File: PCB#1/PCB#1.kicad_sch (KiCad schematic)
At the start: 30 parts, among them J2 Conn_01x02, J3 Conn_02x18_Odd_Even, J4 Conn_02x18_Odd_Even, P1 USB_C_Plug_USB2.0, U1 RP2040, U2 ICM-20948, U3 NCP1117-3.3_SOT223, U4 W25Q128JVS, Y1 Crystal_GND24

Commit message: Add files via upload
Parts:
- added Cd12, Ci2: 10uF, symbol Device:C
- added U5: NCP1117-1.8_SOT223, Package_TO_SOT_SMD:SOT-223-3_TabPin2, symbol Regulator_Linear:NCP1117-1.8_SOT223
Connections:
- net +3.3V: now also Ci2.1, U5.3 (VI); no longer U2.13 (VDD)
- net +3V3: now also U2.13 (VDD)
- net GND: now also Cd12.2, Ci2.2, U5.1 (GND)
- net +1V8: now reaches U2.8 (VDDIO)
- net +1V8: now also Cd12.1, U5.2 (VO)
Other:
- note added: "Input Supply Converts 3.3v to 1.8v"

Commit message: Add files via upload
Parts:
- removed Cd2: 10uF, symbol Device:C
- removed J3, J4: Conn_02x18_Odd_Even, symbol Connector_Generic:Conn_02x18_Odd_Even
- added Cd13, Cd14, Cd15: 100nF, symbol Device:C
- added Cd16: 10uF, symbol Device:C
- added Q1: BSS138, Package_TO_SOT_SMD:SOT-23, symbol Transistor_FET:BSS138
- added R6, R7: 4.7k, symbol Device:R
- added U6: ISO1540, Package_SO:SOIC-8_3.9x4.9mm_P1.27mm, symbol Isolator:ISO1540
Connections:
- net GND is gone; now on net +1V8: Cc1.2, Cc2.2, Cd1.2, Cd10.2, Cd11.2, Cd12.2, Cd2.2, Cd3.2, Cd4.2, Cd5.2, Cd6.2, Cd7.2, Cd8.2, Cd9.2, Cf1.2, Ci1.2, Ci2.2, J2.2 (Pin_2), P1.A1 (GND), P1.A12 (GND), P1.B1 (GND), P1.B12 (GND), P1.S1 (SHIELD), R5.2, U1.57 (GND), U2.18 (GND), U2.20 (GND), U3.1 (GND), U4.4 (GND), U5.1 (GND), Y1.2, Y1.4
- net +1V8: now also U2.9 (SDO/AD0), Cd13.2, Cd14.1, Cd14.2, Cd15.2, Cd16.2, Q1.1 (G), R7.1, U6.4 (GND1), U6.5 (GND2), U6.8 (VCC2)
- net +3V3: now also Cd13.1, Cd16.1, U6.1 (VCC1)
- net at U2.10 (REGOUT): now also Cd15.1
- net at U2.22 (~{CS}): now also R7.2
- new net: Q1.2 (S), R6.1
- no-connect marks 1 -> 6
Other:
- note added: "Address to 0x68"
- note added: "Any GPIO"
- note added: "Data Level Shifter 1v8 to 3v3"
- note added: "I2C mode"
- note added: "INT"
- note added: "Interupt Level Shifter"
- note added: "SCL"
- note added: "SDA"
- moved on the sheet: Cc1, Cc2, Cd1, Cd10, Cd11, Cd2, Cd3, Cd4, Cd5, Cd6, Cd7, Cd8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

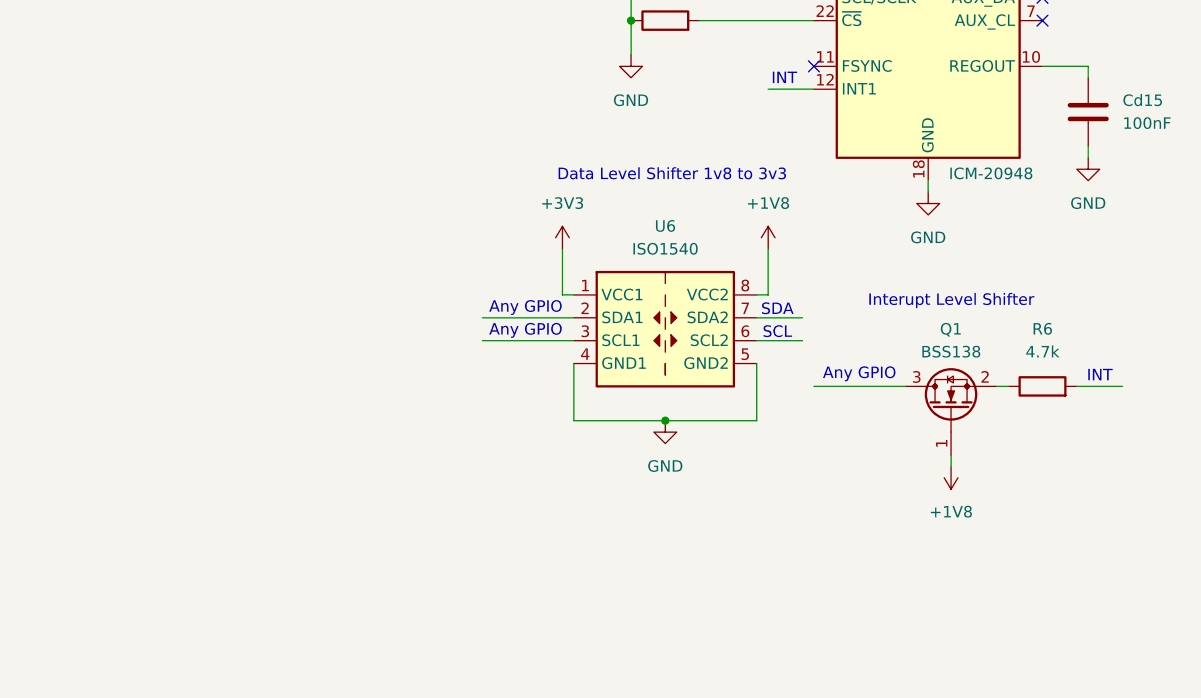
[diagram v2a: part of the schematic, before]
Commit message: Add files via upload
Fixed pull ups
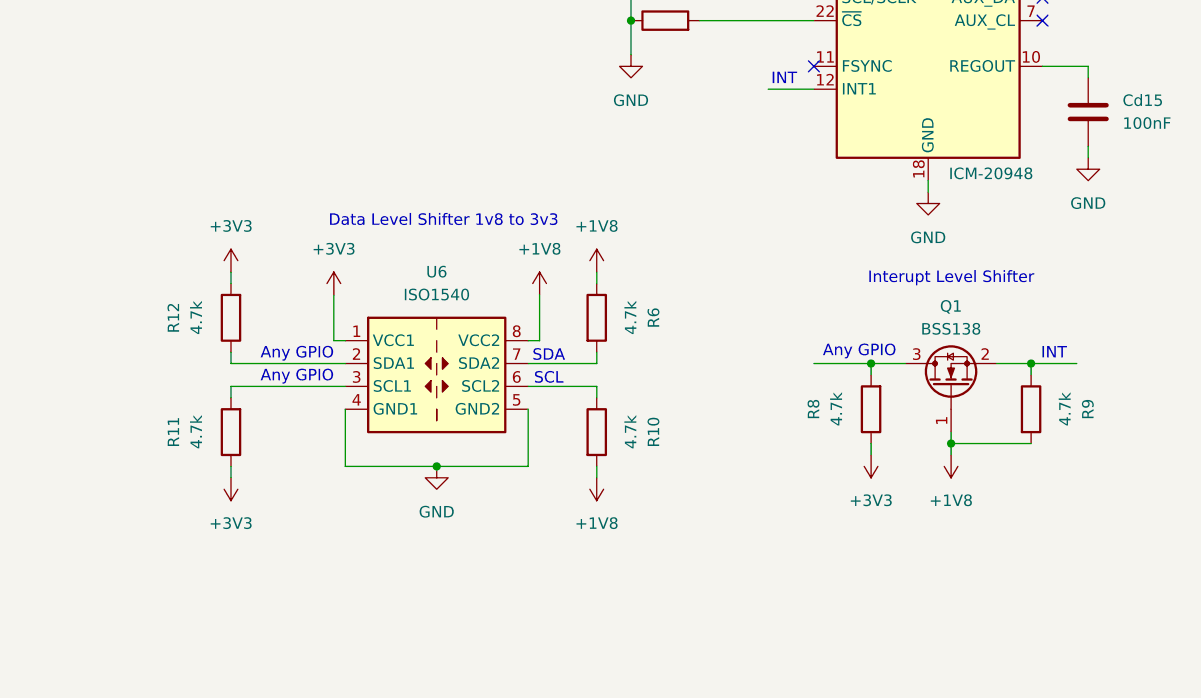
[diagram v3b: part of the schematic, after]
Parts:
- added R10, R11, R12, R8, R9: 4.7k, symbol Device:R
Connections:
- net +1V8: now also R6.1, R10.2, R9.2
- net +3V3: now also R11.1, R12.2, R8.1
- net at Q1.2 (S): now also R9.1; no longer R6.1
- net at Q1.3 (D): now also R8.2
- net at U6.2 (SDA1): now also R12.1
- net at U6.3 (SCL1): now also R11.2
- net at U6.6 (SCL2): now also R10.1
- net at U6.7 (SDA2): now also R6.2
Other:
- moved on the sheet: Q1, U6

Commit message: Add files via upload
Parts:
- removed R10, R11, R12, R6: 4.7k, symbol Device:R
- removed U6: ISO1540, Package_SO:SOIC-8_3.9x4.9mm_P1.27mm, symbol Isolator:ISO1540
- added Cd17, Cd18: 1uF, symbol Device:C
- added R13, R14, R15, R16: 4.7k, symbol Device:R
- added U7: MPL115A1, Package_LGA:NXP_LGA-8_3x5mm_P1.25mm_H1.2mm, symbol Sensor_Pressure:MPL115A1
- added U8: TCA9406DC, symbol Interface:TCA9406DC
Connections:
- net +1V8: now also U1.19 (TESTEN), Cd17.2, Cd18.2, R15.1, R16.2, U7.3 (GND), U8.2 (GND), U8.3 (VCCA), U8.6 (OE)
- net +3V3: now also Cd17.1, R13.2, R14.1, U7.1 (VDD), U8.7 (VCCB)
- new net: R13.1, U8.1 (SDA_B)
- new net: Cd18.1, U7.2 (CAP)
- new net: R14.2, U8.8 (SCL_B)
- new net: R15.2, U8.4 (SDA_A)
- new net: R16.1, U8.5 (SCL_A)
- no-connect marks 6 -> 7
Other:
- note added: "VDD"

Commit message: Add files via upload
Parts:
- added C24: 100nF, Capacitor_SMD:C_0603_1608Metric, symbol Device:C
- added R6: 27.4, Resistor_SMD:R_0603_1608Metric, symbol Device:R
- C1: renamed from Ci1; footprint (none) -> Capacitor_SMD:C_0603_1608Metric
- C10: renamed from Cd6; footprint (none) -> Capacitor_SMD:C_0603_1608Metric
- C11: renamed from Cd4; footprint (none) -> Capacitor_SMD:C_0603_1608Metric
- C12: renamed from Cd7; footprint (none) -> Capacitor_SMD:C_0603_1608Metric
- C13: renamed from Cd8; footprint (none) -> Capacitor_SMD:C_0603_1608Metric
- C14: renamed from Cd9; footprint (none) -> Capacitor_SMD:C_0603_1608Metric
- C15: renamed from Cd10; footprint (none) -> Capacitor_SMD:C_0603_1608Metric
- C16: renamed from Cd17; footprint (none) -> Capacitor_SMD:C_0603_1608Metric
- C17: renamed from Cd11; footprint (none) -> Capacitor_SMD:C_0603_1608Metric
- C18: renamed from Cd18; footprint (none) -> Capacitor_SMD:C_0603_1608Metric
- C19: renamed from Ci2; footprint (none) -> Capacitor_SMD:C_0603_1608Metric
- C2: renamed from Cc1; footprint (none) -> Capacitor_SMD:C_0603_1608Metric
- C20: renamed from Cd14; footprint (none) -> Capacitor_SMD:C_0603_1608Metric
- C21: renamed from Cd13; footprint (none) -> Capacitor_SMD:C_0603_1608Metric
- C22: renamed from Cd12; footprint (none) -> Capacitor_SMD:C_0603_1608Metric
- C23: renamed from Cd15; footprint (none) -> Capacitor_SMD:C_0603_1608Metric
- C3: renamed from Cc2; footprint (none) -> Capacitor_SMD:C_0603_1608Metric
- C4: renamed from Cd16; footprint (none) -> Capacitor_SMD:C_0603_1608Metric
- C5: renamed from Cf1; footprint (none) -> Capacitor_SMD:C_0603_1608Metric
- C6: renamed from Cd3; footprint (none) -> Capacitor_SMD:C_0603_1608Metric
- C7: renamed from Cd2; footprint (none) -> Capacitor_SMD:C_0603_1608Metric
- C8: renamed from Cd1; footprint (none) -> Capacitor_SMD:C_0603_1608Metric
- C9: renamed from Cd5; footprint (none) -> Capacitor_SMD:C_0603_1608Metric
- J2: footprint (none) -> Connector_PinHeader_2.54mm:PinHeader_1x02_P2.54mm_Vertical
- P1: footprint (none) -> Connector_USB:USB_C_Receptacle_HRO_TYPE-C-31-M-12
- R1, R13, R14, R15, R16, R2, R3, R4, R5, R7, R8, R9: footprint (none) -> Resistor_SMD:R_0603_1608Metric
- U8: footprint (none) -> Package_SO:VSSOP-8_3x3mm_P0.65mm
- Y1: footprint (none) -> Crystal:Crystal_SMD_Abracon_ABM8G-4Pin_3.2x2.5mm
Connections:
- net +1V8: no longer C1.2, C10.2, C11.2, C12.2, C13.2, C14.2, C15.2, C16.2, C17.2, C18.2, C19.2, C2.2, C20.2, C21.2, C22.2, C23.2, C3.2, C4.2, C5.2, C6.2, C7.2, C8.2, C9.2, J2.2 (Pin_2), P1.A1 (GND), P1.A12 (GND), P1.B1 (GND), P1.B12 (GND), P1.S1 (SHIELD), R5.2, U1.19 (TESTEN), U1.57 (GND), U2.18 (GND), U2.20 (GND), U2.9 (SDO/AD0), U3.1 (GND), U4.4 (GND), U5.1 (GND), U7.3 (GND), U8.2 (GND), Y1.2, Y1.4
- net +3V3: now also U1.56 (QSPI_SS), U7.4 (~{SHDN}), C24.1, R6.1
- net INT: now reaches U2.12 (INT1)
- net INT: now also Q1.2 (S), R9.1
- net SCL: now reaches U2.23 (SCL/SCLK)
- net SCL: now also R16.1, U8.5 (SCL_A)
- net SDA: now reaches U2.24 (SDA/SDI)
- net SDA: now also R15.2, U8.4 (SDA_A)
- net XIN: now reaches C2.1, Y1.1
- net XIN: now also U1.20 (XIN)
- net GPIO16: now reaches R13.1, U8.1 (SDA_B)
- net GPIO16: now also U1.27 (GPIO16)
- net USB_DP: now reaches P1.A6 (D+)
- net USB_DP: now also R1.1, R6.2
- net USB_DM: now reaches P1.A7 (D-)
- net USB_DM: now also R2.1
- net GPIO13: now reaches U7.5 (~{CS})
- net GPIO13: now also U1.16 (GPIO13)
- net GPIO12: now reaches U7.6 (DOUT)
- net GPIO12: now also U1.15 (GPIO12)
- net GPIO9: now reaches U7.7 (DIN)
- net GPIO9: now also U1.12 (GPIO9)
- net GPIO8: now reaches U7.8 (SCLK)
- net GPIO8: now also U1.11 (GPIO8)
- net QSPI_SD1: now reaches U4.2 (DO/IO_{1})
- net QSPI_SD1: now also U1.55 (QSPI_SD1)
- net QSPI_SD2: now reaches U4.3 (~{WP}/IO_{2})
- net QSPI_SD2: now also U1.54 (QSPI_SD2)
- net QSPI_SD0: now reaches U4.5 (DI/IO_{0})
- net QSPI_SD0: now also U1.53 (QSPI_SD0)
- net QSPI_SCLK: now reaches U4.6 (CLK)
- net QSPI_SCLK: now also U1.52 (QSPI_SCLK)
- net QSPI_SD3: now reaches U4.7 (~{HOLD}/~{RESET}/IO_{3})
- net QSPI_SD3: now also U1.51 (QSPI_SD3)
- net GPIO18: now reaches Q1.3 (D), R8.2
- net GPIO18: now also U1.29 (GPIO18)
- net GPIO17: now reaches R14.2, U8.8 (SCL_B)
- net GPIO17: now also U1.28 (GPIO17)
- net XOUT: now reaches R4.2
- net XOUT: now also U1.21 (XOUT)
- net GPIO14: now reaches U1.17 (GPIO14)
- new net GND: C1.2, C10.2, C11.2, C12.2, C13.2, C14.2, C15.2, C16.2, C17.2, C18.2, C19.2, C2.2, C20.2, C21.2, C22.2, C23.2, C24.2, C3.2, C4.2, C5.2, C6.2, C7.2, C8.2, C9.2, J2.2 (Pin_2), P1.A1 (GND), P1.A12 (GND), P1.B1 (GND), P1.B12 (GND), P1.S1 (SHIELD), R5.2, U1.19 (TESTEN), U1.57 (GND), U2.18 (GND), U2.20 (GND), U2.9 (SDO/AD0), U3.1 (GND), U4.4 (GND), U5.1 (GND), U7.3 (GND), U8.2 (GND), Y1.2, Y1.4
- no-connect marks 7 -> 29
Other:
- note removed: "Any GPIO"
- note removed: "INT"
- note removed: "QSPI_SCLK"
- note removed: "QSPI_SD0"
- note removed: "QSPI_SD1"
- note removed: "QSPI_SD2"
- note removed: "QSPI_SD3"
- note removed: "QSPI_SS"
- note removed: "SCL"
- note removed: "SDA"
- note removed: "USB_DM"
- note removed: "USB_DP"
- note removed: "VDD"
- note removed: "XIN"
- note removed: "XOUT"
- moved on the sheet: C10, C11, C12, C13, C14, C15, C16, C17, C18, C6, C7, C8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

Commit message: Add files via upload
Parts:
- Q1: value BSS138 -> onsemi BSS138
- U1: value RP2040 -> Raspberry Pi RP2040
- U2: value ICM-20948 -> TDK InvenSense ICM-20948
- U3: value NCP1117-3.3_SOT223 -> onsemi NCP1117DT33G
- U4: value W25Q128JVS -> Winbond W25Q128JVSIQ
- U5: value NCP1117-1.8_SOT223 -> onsemi NCP1117DT33G
- U6: renamed from U8; value TCA9406DC -> TI TCA9406DCTR
- U7: value MPL115A1 -> NXP MPL115A1T1
- Y1: value Crystal_GND24 -> ABRACON ABM8-272-T3
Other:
- moved on the sheet: R15, R16
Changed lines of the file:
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@@
 	(wire
 		(pts
-			(xy 198.12 142.24) (xy 198.12 143.51)
+			(xy 201.93 142.24) (xy 201.93 143.51)
 		)
 		(stroke
@@
 	(wire
 		(pts
-			(xy 198.12 151.13) (xy 198.12 152.4)
+			(xy 201.93 151.13) (xy 201.93 152.4)
 		)
 		(stroke
@@
 	(wire
 		(pts
-			(xy 198.12 138.43) (xy 198.12 139.7)
+			(xy 201.93 138.43) (xy 201.93 139.7)
 		)
 		(stroke
@@
 	(wire
 		(pts
-			(xy 198.12 129.54) (xy 198.12 130.81)
+			(xy 201.93 129.54) (xy 201.93 130.81)
 		)
 		(stroke
@@
 	(wire
 		(pts
-			(xy 190.5 139.7) (xy 198.12 139.7)
+			(xy 190.5 139.7) (xy 201.93 139.7)
 		)
 		(stroke
@@
 	(wire
 		(pts
-			(xy 190.5 142.24) (xy 198.12 142.24)
+			(xy 190.5 142.24) (xy 201.93 142.24)
 		)
 		(stroke
@@
 			)
 		)
-		(property "Value" "ICM-20948"
-			(at 258.826 126.238 0)
+		(property "Value" "TDK InvenSense ICM-20948"
+			(at 226.06 125.984 0)
 			(effects
 				(font
@@
 			)
 		)
-		(property "Value" "Crystal_GND24"
+		(property "Value" "ABRACON ABM8-272-T3"
 			(at 45.72 168.656 90)
 			(effects
@@
 			)
 		)
-		(property "Value" "NCP1117-1.8_SOT223"
+		(property "Value" "onsemi NCP1117DT33G"
 			(at 260.35 27.94 0)
 			(effects
@@
 			)
 		)
-		(property "Value" "MPL115A1"
-			(at 189.23 104.394 0)
+		(property "Value" "NXP MPL115A1T1"
+			(at 171.958 104.394 0)
 			(effects
 				(font
@@
 			)
 		)
-		(property "Value" "W25Q128JVS"
-			(at 62.738 148.59 0)
+		(property "Value" "Winbond W25Q128JVSIQ"
+			(at 34.544 148.59 0)
 			(effects
 				(font
@@
 			)
 		)
-		(property "Value" "BSS138"
+		(property "Value" "onsemi BSS138"
 			(at 259.08 143.51 90)
 			(effects
@@
 		(on_board yes)
 		(dnp no)
-		(property "Reference" "U8"
+		(property "Reference" "U6"
 			(at 185.42 130.302 0)
 			(effects
@@
 			)
 		)
-		(property "Value" "TCA9406DC"
-			(at 184.404 153.924 0)
+		(property "Value" "TI TCA9406DCTR"
+			(at 184.404 154.178 0)
 			(effects
 				(font
@@
 			(project "PCB#1"
 				(path "/c3c628a5-133e-4c45-8bc2-234ddb9bbbb2"
-					(reference "U8")
+					(reference "U6")
 					(unit 1)
 				)
@@
 	(symbol
 		(lib_id "Device:R")
-		(at 198.12 147.32 0)
+		(at 201.93 147.32 0)
 		(unit 1)
 		(exclude_from_sim no)
@@
 		(dnp no)
 		(property "Reference" "R16"
-			(at 204.47 147.32 90)
+			(at 208.28 147.32 90)
 			(effects
 				(font
@@
 		)
 		(property "Value" "4.7k"
-			(at 201.93 147.32 90)
+			(at 205.74 147.32 90)
 			(effects
 				(font
@@
 		)
 		(property "Footprint" "Resistor_SMD:R_0603_1608Metric"
-			(at 196.342 147.32 90)
+			(at 200.152 147.32 90)
 			(effects
 				(font
@@
 		)
 		(property "Datasheet" "~"
-			(at 198.12 147.32 0)
+			(at 201.93 147.32 0)
 			(effects
 				(font
@@
 		)
 		(property "Description" "Resistor"
-			(at 198.12 147.32 0)
+			(at 201.93 147.32 0)
 			(effects
 				(font
@@
 	(symbol
 		(lib_id "Device:R")
-		(at 198.12 134.62 0)
+		(at 201.93 134.62 0)
 		(unit 1)
 		(exclude_from_sim no)
@@
 		(dnp no)
 		(property "Reference" "R15"
-			(at 204.47 134.62 90)
+			(at 208.28 134.62 90)
 			(effects
 				(font
@@
 		)
 		(property "Value" "4.7k"
-			(at 201.93 134.62 90)
+			(at 205.74 134.62 90)
 			(effects
 				(font
@@
 		)
 		(property "Footprint" "Resistor_SMD:R_0603_1608Metric"
-			(at 196.342 134.62 90)
+			(at 200.152 134.62 90)
 			(effects
 				(font
@@
 		)
 		(property "Datasheet" "~"
-			(at 198.12 134.62 0)
+			(at 201.93 134.62 0)
 			(effects
 				(font
@@
 		)
 		(property "Description" "Resistor"
-			(at 198.12 134.62 0)
+			(at 201.93 134.62 0)
 			(effects
 				(font
@@
 			)
 		)
-		(property "Value" "RP2040"
-			(at 128.27 146.304 0)
+		(property "Value" "Raspberry Pi RP2040"
+			(at 119.634 146.304 0)
 			(effects
 				(font
@@
 	(symbol
 		(lib_id "power:+1V8")
-		(at 198.12 152.4 180)
+		(at 201.93 152.4 180)
 		(unit 1)
 		(exclude_from_sim no)
@@
 		(fields_autoplaced yes)
 		(property "Reference" "#PWR056"
-			(at 198.12 148.59 0)
+			(at 201.93 148.59 0)
 			(effects
 				(font
@@
 		)
 		(property "Value" "+1V8"
-			(at 198.12 157.48 0)
+			(at 201.93 157.48 0)
 			(effects
 				(font
@@
 		)
 		(property "Footprint" ""
-			(at 198.12 152.4 0)
+			(at 201.93 152.4 0)
 			(effects
 				(font
@@
 		)
 		(property "Datasheet" ""
-			(at 198.12 152.4 0)
+			(at 201.93 152.4 0)
 			(effects
 				(font
@@
 		)
 		(property "Description" "Power symbol creates a global label with name \"+1V8\""
-			(at 198.12 152.4 0)
+			(at 201.93 152.4 0)
 			(effects
 				(font
@@
 			)
 		)
-		(property "Value" "NCP1117-3.3_SOT223"
+		(property "Value" "onsemi NCP1117DT33G"
 			(at 35.56 77.47 0)
 			(effects
@@
 	(symbol
 		(lib_id "power:+1V8")
-		(at 198.12 129.54 0)
+		(at 201.93 129.54 0)
 		(unit 1)
 		(exclude_from_sim no)
@@
 		(fields_autoplaced yes)
 		(property "Reference" "#PWR053"
-			(at 198.12 133.35 0)
+			(at 201.93 133.35 0)
 			(effects
 				(font
@@
 		)
 		(property "Value" "+1V8"
-			(at 198.12 124.46 0)
+			(at 201.93 124.46 0)
 			(effects
 				(font
@@
 		)
 		(property "Footprint" ""
-			(at 198.12 129.54 0)
+			(at 201.93 129.54 0)
 			(effects
 				(font
@@
 		)
 		(property "Datasheet" ""
-			(at 198.12 129.54 0)
+			(at 201.93 129.54 0)
 			(effects
 				(font
@@
 		)
 		(property "Description" "Power symbol creates a global label with name \"+1V8\""
-			(at 198.12 129.54 0)
+			(at 201.93 129.54 0)
 			(effects
 				(font
